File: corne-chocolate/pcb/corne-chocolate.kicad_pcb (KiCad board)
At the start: 2 copper layers, 133.8 x 91.4 mm, 98 parts, among them J3 LED, P1 i2c-pin, P2 i2c-pin, SW1 SW_PUSH, SW10 SW_PUSH, SW11 SW_PUSH, SW12 SW_PUSH, SW13 SW_PUSH, SW14 SW_PUSH, SW15 SW_PUSH, SW16 SW_PUSH, SW17 SW_PUSH, SW18 SW_PUSH, SW19 SW_PUSH, SW2 SW_PUSH, SW20 SW_PUSH, SW21 SW_PUSH, SW3 SW_PUSH, SW4 SW_PUSH, SW5 SW_PUSH, SW6 SW_PUSH, SW7 SW_PUSH, SW8 SW_PUSH, SW9 SW_PUSH, U1 ProMicro

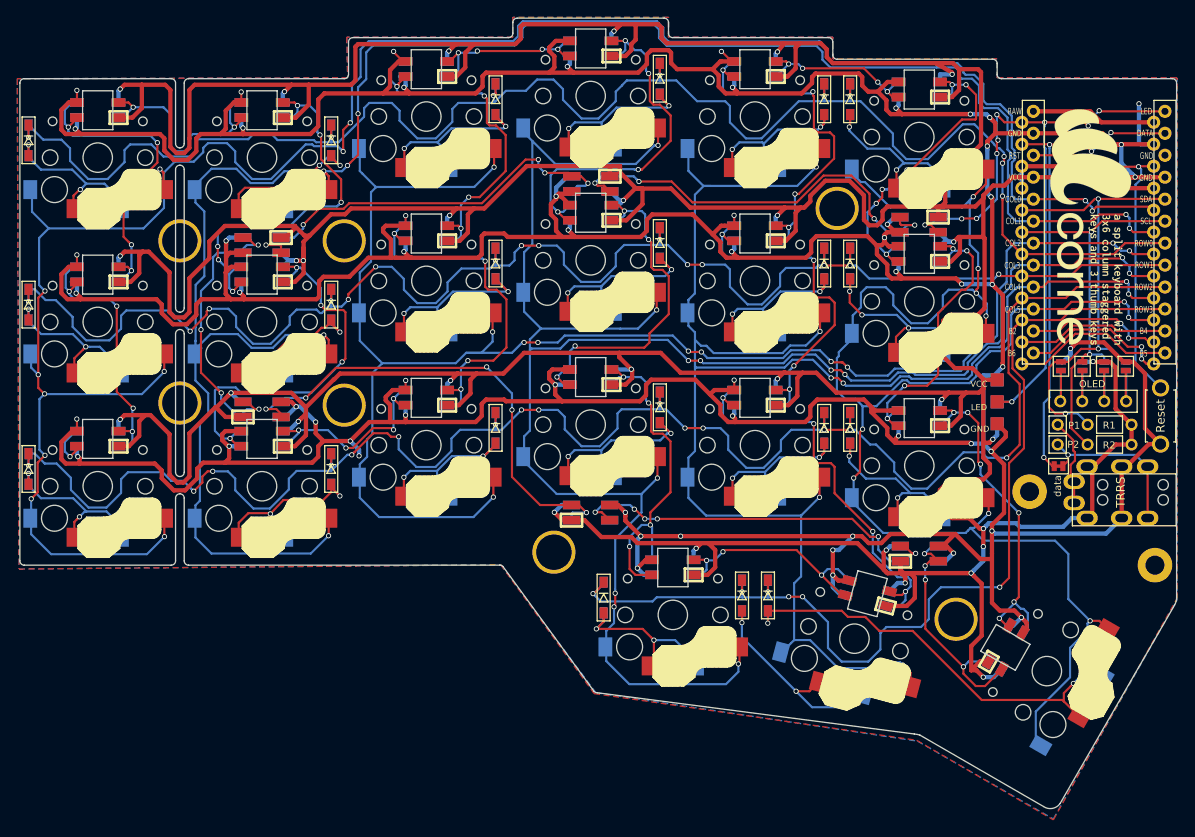
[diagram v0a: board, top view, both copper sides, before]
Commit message: Made outermost thumb button removable. Rewired to expose SCLK, MOSI, and MISO pins. Routed trackball pins and exposed pads. Added battery/power switch mount points.
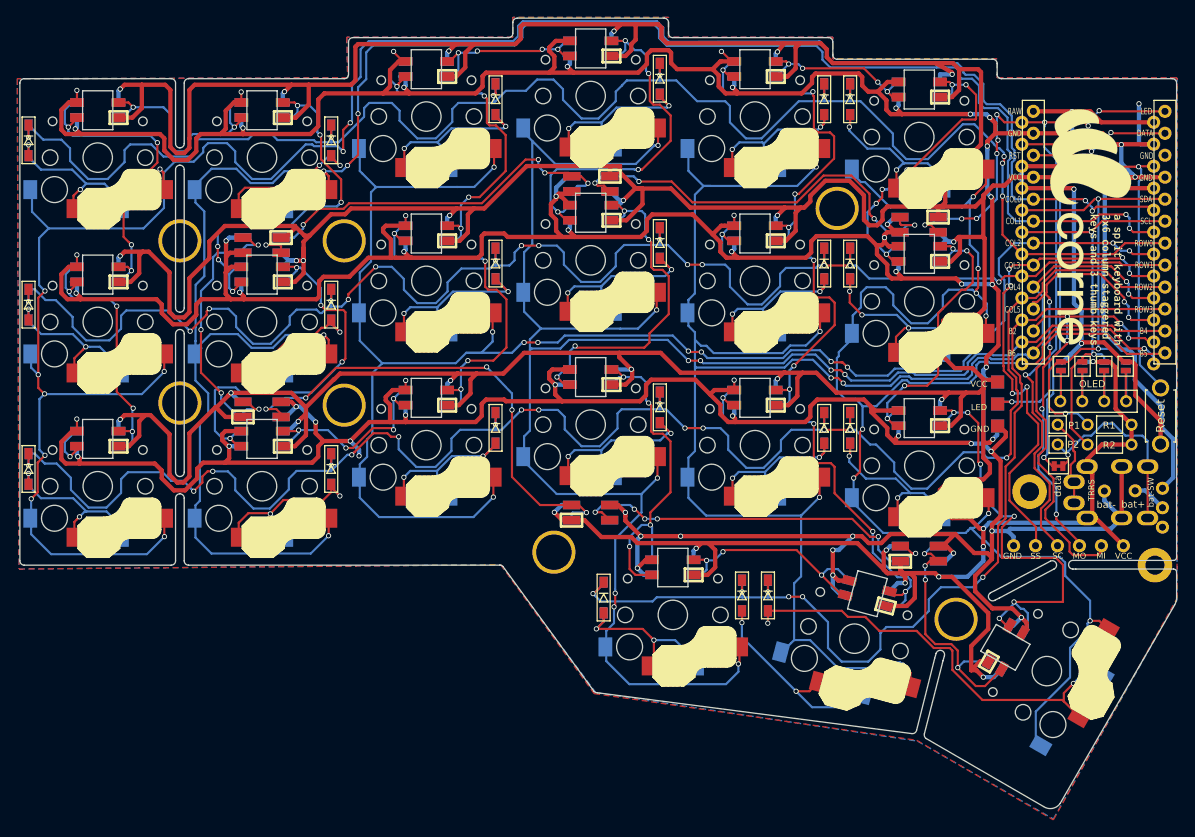
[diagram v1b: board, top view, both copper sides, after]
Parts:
- removed TRRS: MJ-4PP-9, kbd:MJ-4PP-9
- added ?: , , F.Cu at (182.9, 114.6)
- added ?: , , F.Cu at (186.4, 115.7)
- added ?: , , F.Cu at (188.4, 112.8)
- added ?: , , F.Cu at (184.4, 118.8)
- added ?: , , F.Cu at (190.0, 115.7)
- added ?: , , F.Cu at (193.1, 117.6)
- added ?: , , F.Cu at (191.4, 118.8)
- added ?: , , F.Cu at (182.9, 117.0)
- added ?: , , F.Cu at (178.4, 122.0)
- added ?: , , F.Cu at (193.1, 115.4)
- added ?: , , F.Cu at (188.4, 118.8)
- added ?: , , F.Cu at (175.9, 122.0)
- added ?: , , F.Cu at (188.6, 122.0)
- added ?: , , F.Cu at (181.0, 122.0)
- added ?: , , F.Cu at (191.4, 112.8)
- added ?: , , F.Cu at (183.5, 122.0)
- added ?: , , F.Cu at (193.1, 119.9)
- added ?: , , F.Cu at (184.4, 112.8)
- added ?: , , F.Cu at (186.1, 122.0)
- moved J3 0.25 mm to (174.1, 108.2)
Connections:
- U1 pad 11: Net-(U1-Pad11) -> col3
- U1 pad 12: Net-(U1-Pad12) -> col5
- U1 pad 13: Net-(U1-Pad13) -> col4
- U1 pad 14: Net-(U1-Pad14) -> MO
- U1 pad 15: col5 -> MI
- U1 pad 16: col4 -> SC
- U1 pad 17: col3 -> SS
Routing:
- net MI: track 0.00 -> 58.5 mm, vias 0 -> 4
- net SS: track 0.00 -> 57.4 mm, vias 0 -> 6
- net SC: track 0.00 -> 51.8 mm, vias 0 -> 3
- net Net-(U1-Pad24): track 14.4 -> 64.0 mm, vias 0 -> 1
- net MO: track 0.00 -> 46.6 mm, vias 0 -> 6
- net GND: track 816.7 -> 841.5 mm, vias 59 -> 60
- net Net-(U1-Pad12): track 18.9 -> 0.00 mm
- net Net-(U1-Pad11): track 17.6 -> 0.00 mm
- net Net-(U1-Pad13): track 17.5 -> 0.00 mm, vias 2 -> 0
- net Net-(U1-Pad14): track 16.0 -> 0.00 mm, vias 2 -> 0
- net Net-(L18-Pad3): track 39.1 -> 52.5 mm
- net VCC: track 786.4 -> 796.0 mm
- net col3: track 224.8 -> 217.8 mm, vias 12 -> 10
- net Net-(J1-PadB): track 19.0 -> 23.9 mm
- net BAT+: track 0.00 -> 4.38 mm
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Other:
- outline, holes or cut-outs redrawn
- net class Default removed
- rule pad_to_mask_clearance: 0.2 -> 0
- board text added: "Corne Chocolate Gimmin TB Mod v1.1 PCB: foostan, Mod: Gimmin"
- board text added: "MI"
- board text added: "MO"
- board text added: "SC"
- board text added: "SS"
- board text added: "TRRS"
- board text added: "bat SW"
- board text added: "bat+"
- board text added: "bat-"
- board text added: "bat-SW"
- board text removed: "Corne Chocolate v2.1 PCB designed by foostan"
